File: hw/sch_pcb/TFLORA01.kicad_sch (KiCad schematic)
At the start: 51 parts, among them J1 SM07B-GHS-TB, J2 MCX, U1 MIC5504-3.3YM5, U2 74LVC1G157, U3 SX1262, U4 PE4259, X1 IT3205CE 32MHz

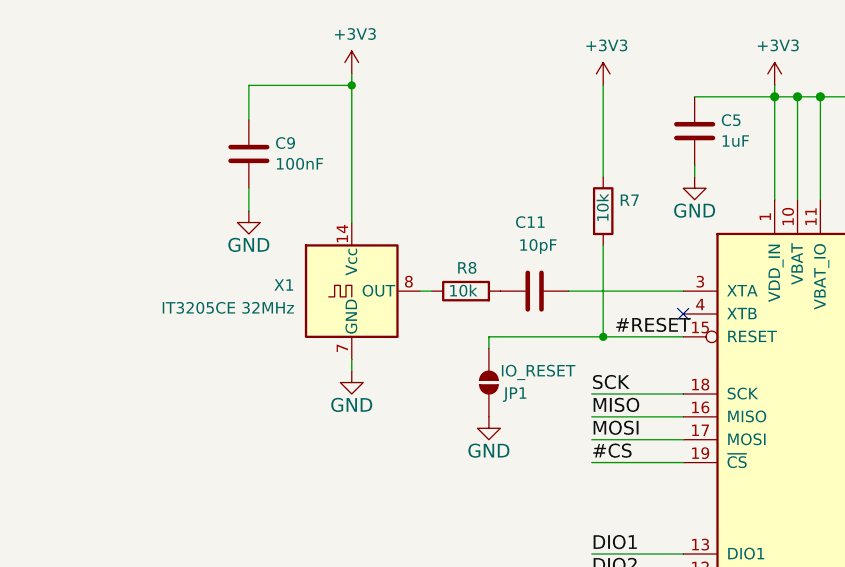
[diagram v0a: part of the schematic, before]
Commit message: Resolve #3 by selecting oscillator.
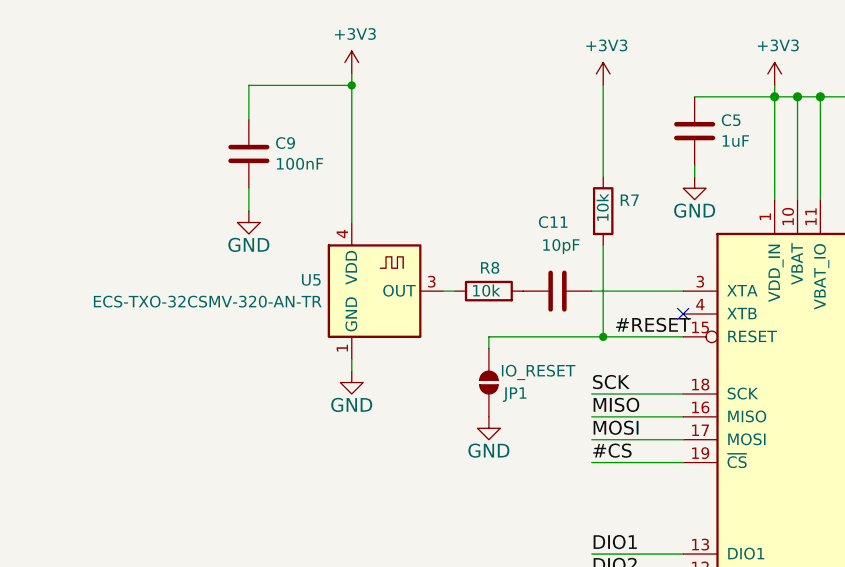
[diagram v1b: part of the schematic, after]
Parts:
- removed X1: IT3205CE 32MHz, Oscillator:Oscillator_DIP-14, symbol Oscillator:TCXO-14
- added U5: ECS-TXO-32CSMV-320-AN-TR, Oscillator:Oscillator_SMD_Abracon_ASE-4Pin_3.2x2.5mm, symbol Oscillator:FT5HN
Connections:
- net +3V3: now also U5.4 (VDD)
- net GND: now also U5.1 (GND), U5.2 (GND)
- net at R8.1: now also U5.3 (OUT)
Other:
- moved on the sheet: C11, R8
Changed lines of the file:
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@@
 	(wire
 		(pts
-			(xy 76.2 91.44) (xy 63.5 91.44)
+			(xy 76.2 91.44) (xy 66.04 91.44)
 		)
 		(stroke
@@
 	(wire
 		(pts
-			(xy 46.99 91.44) (xy 48.26 91.44)
+			(xy 49.53 91.44) (xy 50.8 91.44)
 		)
 		(stroke
@@
 	(symbol
 		(lib_id "ISM02A-rescue:C-Device-ISM02A-rescue")
-		(at 59.69 91.44 90)
+		(at 62.23 91.44 90)
 		(unit 1)
 		(exclude_from_sim no)
@@
 		(dnp no)
 		(property "Reference" "C11"
-			(at 60.96 83.82 90)
+			(at 63.5 83.82 90)
 			(effects
 				(font
@@
 		)
 		(property "Value" "10pF"
-			(at 62.23 86.36 90)
+			(at 64.77 86.36 90)
 			(effects
 				(font
@@
 		)
 		(property "Footprint" "Capacitor_SMD:C_0603_1608Metric"
-			(at 63.5 90.4748 0)
+			(at 66.04 90.4748 0)
 			(effects
 				(font
@@
 		)
 		(property "Datasheet" "~"
-			(at 59.69 91.44 0)
+			(at 62.23 91.44 0)
 			(effects
 				(font
@@
 		)
 		(property "Description" ""
-			(at 59.69 91.44 0)
+			(at 62.23 91.44 0)
 			(effects
 				(font
@@
 	(symbol
 		(lib_id "ISM02A-rescue:R-Device-ISM02A-rescue")
-		(at 52.07 91.44 90)
+		(at 54.61 91.44 90)
 		(unit 1)
 		(exclude_from_sim no)
@@
 		(dnp no)
 		(property "Reference" "R8"
-			(at 53.34 88.9 90)
+			(at 55.88 88.9 90)
 			(effects
 				(font
@@
 		)
 		(property "Value" "10k"
-			(at 53.34 91.44 90)
+			(at 55.88 91.44 90)
 			(effects
 				(font
@@
 		)
 		(property "Footprint" "Resistor_SMD:R_0603_1608Metric"
-			(at 52.07 93.218 90)
+			(at 54.61 93.218 90)
 			(effects
 				(font
@@
 		)
 		(property "Datasheet" "~"
-			(at 52.07 91.44 0)
+			(at 54.61 91.44 0)
 			(effects
 				(font
@@
 		)
 		(property "Description" ""
-			(at 52.07 91.44 0)
+			(at 54.61 91.44 0)
 			(effects
 				(font
@@
 		)
 		(property "UST_ID" "5c70984512875079b91f8962"
-			(at 135.89 182.88 0)
+			(at 138.43 182.88 0)
 			(effects
 				(font
@@
 	)
 	(symbol
+		(lib_id "Oscillator:FT5HN")
+		(at 41.91 91.44 0)
+		(unit 1)
+		(exclude_from_sim no)
+		(in_bom yes)
+		(on_board yes)
+		(dnp no)
+		(fields_autoplaced yes)
+		(property "Reference" "U5"
+			(at 36.0681 90.2278 0)
+			(effects
+				(font
+					(size 1.27 1.27)
+				)
+				(justify right)
+			)
+		)
+		(property "Value" "ECS-TXO-32CSMV-320-AN-TR"
+			(at 36.0681 92.6521 0)
+			(effects
+				(font
+					(size 1.27 1.27)
+				)
+				(justify right)
+			)
+		)
+		(property "Footprint" "Oscillator:Oscillator_SMD_Abracon_ASE-4Pin_3.2x2.5mm"
+			(at 41.91 107.95 0)
+			(effects
+				(font
+					(size 1.27 1.27)
+				)
+				(hide yes)
+			)
+		)
+		(property "Datasheet" "https://eu.mouser.com/datasheet/2/122/ECS_TXO_32CSMV-1663895.pdf"
+			(at 43.18 110.49 0)
+			(effects
+				(font
+					(size 1.27 1.27)
+				)
+				(hide yes)
+			)
+		)
+		(property "Description" "TCXO Oscillators 32.000 MHz MultiVolt TCXO Clipped Sine Wave 1.7 - 3.465V +/-500ppb -40 - +85C 3.2 x 2.5mm 4-SMD"
+			(at 41.91 91.44 0)
+			(effects
+				(font
+					(size 1.27 1.27)
+				)
+				(hide yes)
+			)
+		)
+		(property "UST_ID" ""
+			(at 41.91 91.44 0)
+			(effects
+				(font
+					(size 1.27 1.27)
+				)
+				(hide yes)
+			)
+		)
+		(pin "2"
+		)
+		(pin "4"
+		)
+		(pin "1"
+		)
+		(pin "3"
+		)
+		(instances
+			(project ""
+				(path "/4497622e-6a35-4d56-b145-e61873b6a125"
+					(reference "U5")
+					(unit 1)
+				)
+			)
+		)
+	)
+	(symbol
 		(lib_id "Device:R")
 		(at 44.45 31.75 90)
@@
 					(unit 1)
 				)
-			)
-		)
-	)
-	(symbol
-		(lib_id "Oscillator:TCXO-14")
-		(at 39.37 91.44 0)
-		(unit 1)
-		(exclude_from_sim no)
-		(in_bom yes)
-		(on_board yes)
-		(dnp no)
-		(fields_autoplaced yes)
-		(property "Reference" "X1"
-			(at 33.02 90.805 0)
-			(effects
-				(font
-					(size 1.27 1.27)
-				)
-				(justify right)
-			)
-		)
-		(property "Value" "IT3205CE 32MHz"
-			(at 33.02 93.345 0)
-			(effects
-				(font
-					(size 1.27 1.27)
-				)
-				(justify right)
-			)
-		)
-		(property "Footprint" "Oscillator:Oscillator_DIP-14"
-			(at 50.8 100.33 0)
-			(effects
-				(font
-					(size 1.27 1.27)
-				)
-				(hide yes)
-			)
-		)
-		(property "Datasheet" "http://www.golledge.com/pdf/products/tcxos/gtxos14.pdf"
-			(at 36.83 91.44 0)
-			(effects
-				(font
-					(size 1.27 1.27)
-				)
-				(hide yes)
-			)
-		)
-		(property "Description" ""
-			(at 39.37 91.44 0)
-			(effects
-				(font
-					(size 1.27 1.27)
-				)
-				(hide yes)
-			)
-		)
-		(pin "1"
-		)
-		(pin "14"
-		)
-		(pin "7"
-		)
-		(pin "8"
-		)
-		(instances
-			(project ""
-				(path "/4497622e-6a35-4d56-b145-e61873b6a125"
-					(reference "X1")
-					(unit 1)
-				)

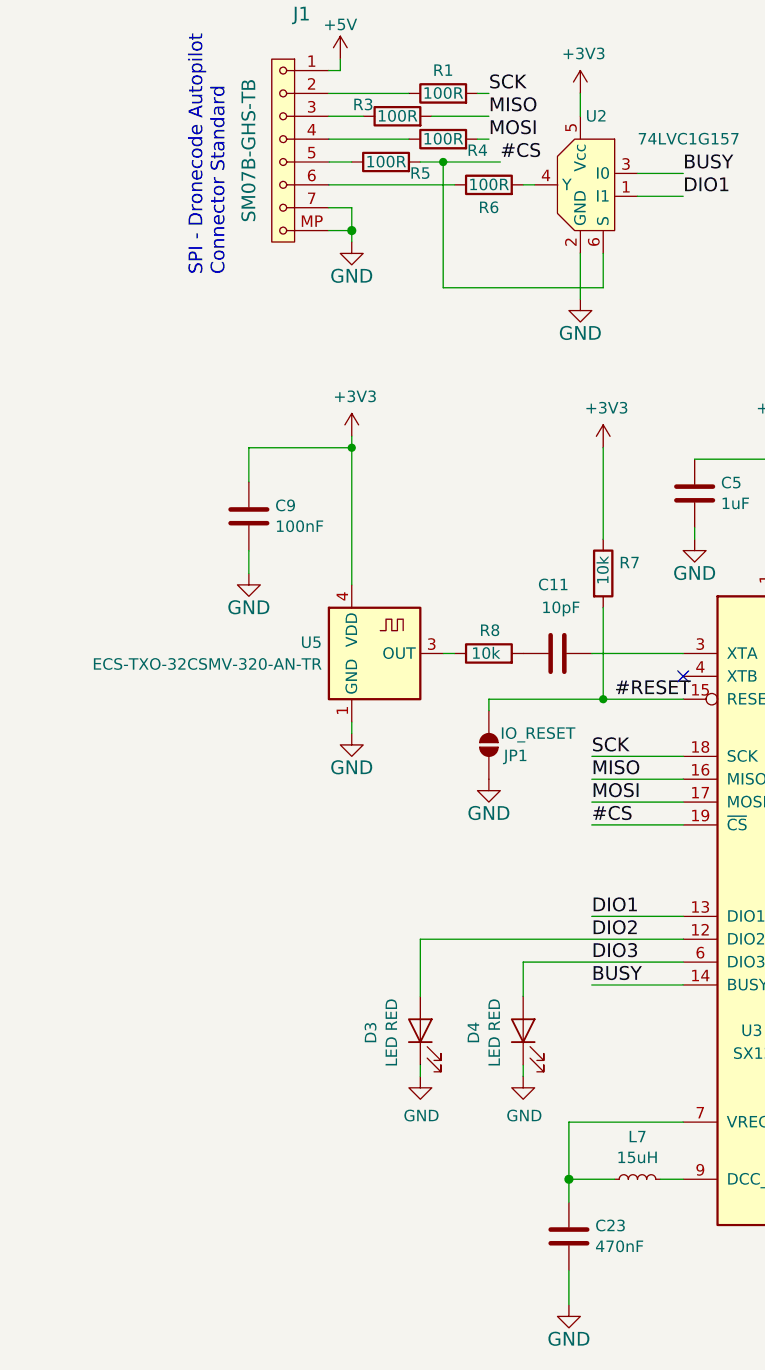
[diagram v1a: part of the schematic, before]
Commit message: Routed PCB, WIP.
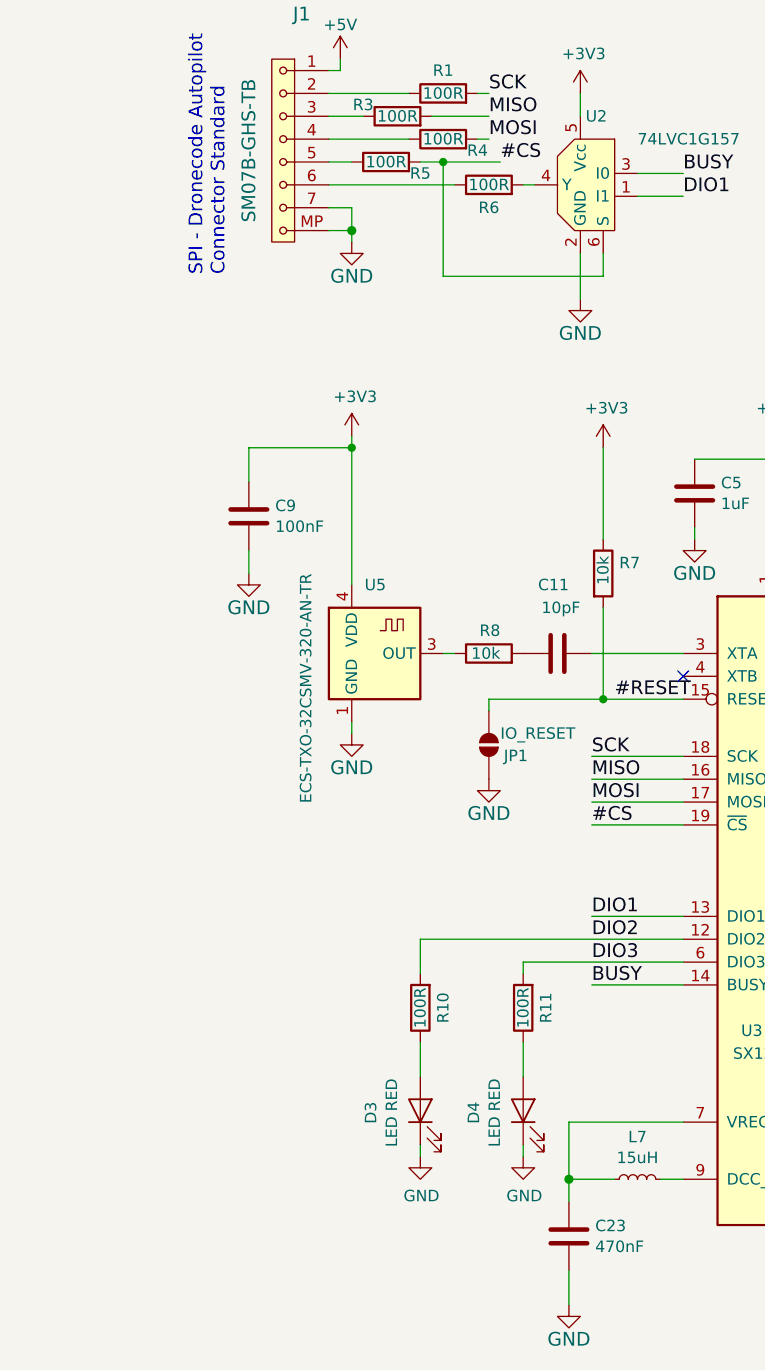
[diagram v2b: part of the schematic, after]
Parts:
- added R10, R11: 100R, Resistor_SMD:R_0603_1608Metric, symbol Device:R
- J2: footprint Mlab_CON:MCX_Molex_73415-1061 -> Mlab_CON:MCX
- JP1: footprint (none) -> Jumper:SolderJumper-2_P1.3mm_Open_RoundedPad1.0x1.5mm
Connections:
- net DIO2: now also R10.2; no longer D3.2 (A)
- net DIO3: now also R11.2; no longer D4.2 (A)
- new net: D4.2 (A), R11.1
- new net: D3.2 (A), R10.1
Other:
- moved on the sheet: D3, D4

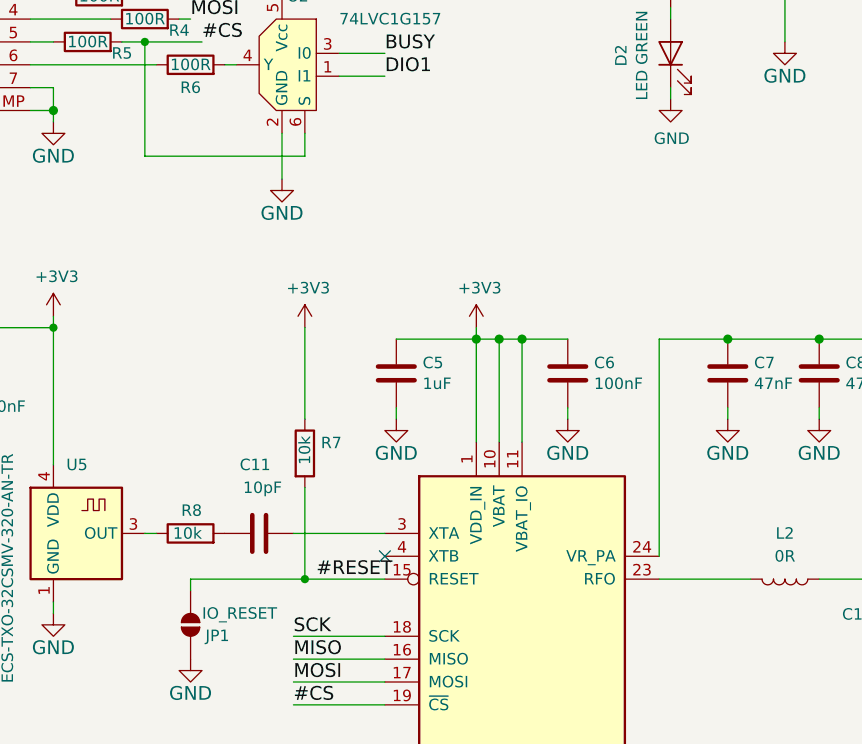
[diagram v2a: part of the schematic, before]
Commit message: Rerouting RF layout. Change 0402 inductors to 0603 for increase of Q.
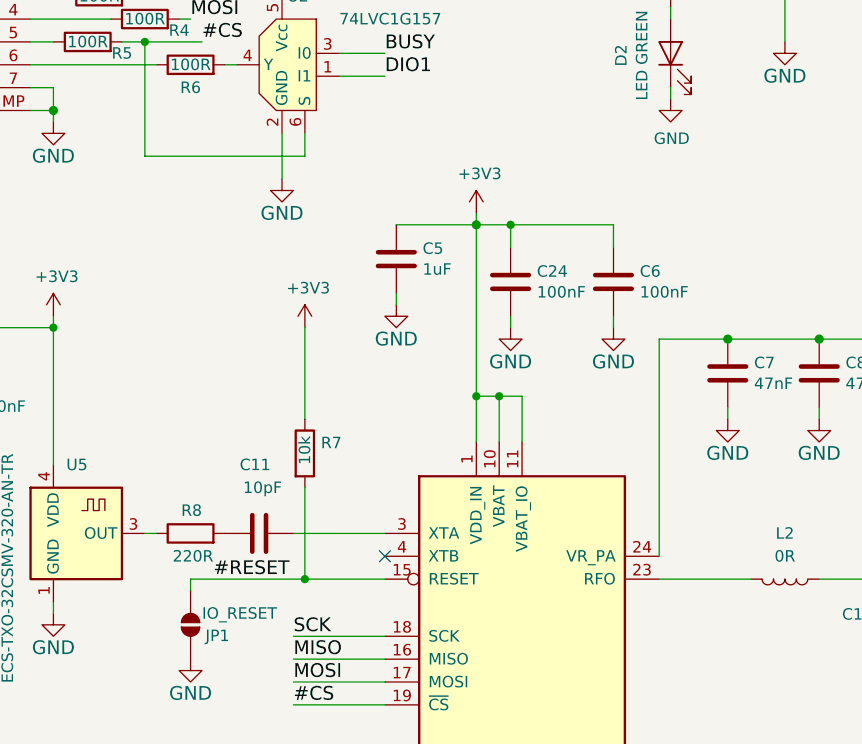
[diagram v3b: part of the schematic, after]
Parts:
- added C24: 100nF, Capacitor_SMD:C_0603_1608Metric, symbol ISM02A-rescue:C-Device-ISM02A-rescue
- L1, L2, L3, L4, L5, L6: footprint Inductor_SMD:L_0402_1005Metric -> Inductor_SMD:L_0603_1608Metric
- R8: value 10k -> 220R
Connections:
- net +3V3: now also C24.1
- net GND: now also C24.2
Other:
- moved on the sheet: C5, C6

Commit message: Adding logo, improving silkscreen. Minor layout improvements. Fix components identification.
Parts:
- added G1: LOGO, MLAB_LOGA:TF, symbol MLAB_TF_LOGO:LOGO
- L1: MFPN LQW15AN47NJ00D -> LQW18AS47NG00D; UST_ID 5dad56ba128750448eca1968 -> 5c70984412875079b91f8813
- L2: UST_ID 5c70984512875079b91f8949 -> 5c70984512875079b91f894e
- L3: value 2n5 -> 2n4; UST_ID 5dad56ff128750448eca1975 -> 67119a34d509c19f2ce8ec7b
- L4: MFPN LQW15AN4N7C00D -> LQW18AN4N7D00D; UST_ID 5dad574f128750448eca1986 -> 671226edd509c19f2ce8ed2d
- L5: MFPN LQW15AN9N1H00D -> LQW18AN9N1D00D; UST_ID 5dad5789128750448eca1995 -> 67122378d509c19f2ce8ecdb
- L6: MFPN LQW15AN15NH00D -> LQW18AN15NJ10D; UST_ID 5dad566c128750448eca1959 -> 671220a9d509c19f2ce8eca2
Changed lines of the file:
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@@
 			)
 		)
-		(property "MFPN" "LQW15AN47NJ00D"
+		(property "MFPN" "LQW18AS47NG00D"
 			(at 133.35 73.66 0)
 			(effects
@@
 			)
 		)
-		(property "UST_ID" "5dad56ba128750448eca1968"
+		(property "UST_ID" "5c70984412875079b91f8813"
 			(at -24.13 148.59 0)
 			(effects
@@
 			)
 		)
-		(property "UST_ID" "5c70984512875079b91f8949"
+		(property "UST_ID" "5c70984512875079b91f894e"
 			(at 218.44 -48.26 0)
 			(effects
@@
 			)
 		)
-		(property "Value" "2n5"
+		(property "Value" "2n4"
 			(at 139.7 99.0346 90)
 			(effects
@@
 			)
 		)
-		(property "UST_ID" "5dad56ff128750448eca1975"
+		(property "UST_ID" "67119a34d509c19f2ce8ec7b"
 			(at 237.49 -67.31 0)
 			(effects
@@
 			)
 		)
-		(property "MFPN" "LQW15AN4N7C00D"
+		(property "MFPN" "LQW18AN4N7D00D"
 			(at 257.81 -87.63 0)
 			(effects
@@
 			)
 		)
-		(property "UST_ID" "5dad574f128750448eca1986"
+		(property "UST_ID" "671226edd509c19f2ce8ed2d"
 			(at 257.81 -87.63 0)
 			(effects
@@
 			)
 		)
-		(property "MFPN" "LQW15AN15NH00D"
+		(property "MFPN" " LQW18AN15NJ10D"
 			(at 252.73 -1.27 0)
 			(effects
@@
 			)
 		)
-		(property "UST_ID" "5dad566c128750448eca1959"
+		(property "UST_ID" "671220a9d509c19f2ce8eca2"
 			(at 252.73 -1.27 0)
 			(effects
@@
 			)
 		)
-		(property "MFPN" "LQW15AN9N1H00D"
+		(property "MFPN" "LQW18AN9N1D00D"
 			(at 327.66 -93.98 0)
 			(effects
@@
 			)
 		)
-		(property "UST_ID" "5dad5789128750448eca1995"
+		(property "UST_ID" "67122378d509c19f2ce8ecdb"
 			(at 327.66 -93.98 0)
 			(effects
@@
 					(unit 1)
 				)
+			)
+		)
+	)
+	(symbol
+		(lib_id "MLAB_TF_LOGO:LOGO")
+		(at 259.08 30.48 0)
+		(unit 1)
+		(exclude_from_sim no)
+		(in_bom no)
+		(on_board yes)
+		(dnp no)
+		(fields_autoplaced yes)
+		(property "Reference" "G1"
+			(at 273.3431 30.959 0)
+			(effects
+				(font
+					(size 1.27 1.27)
+				)
+				(justify left)
+			)
+		)
+		(property "Value" "LOGO"
+			(at 259.08 36.9476 0)
+			(effects
+				(font
+					(size 1.27 1.27)
+				)
+				(hide yes)
+			)
+		)
+		(property "Footprint" "MLAB_LOGA:TF"
+			(at 259.08 30.48 0)
+			(effects
+				(font
+					(size 1.27 1.27)
+				)
+				(hide yes)
+			)
+		)
+		(property "Datasheet" ""
+			(at 259.08 30.48 0)
+			(effects
+				(font
+					(size 1.27 1.27)
+				)
+				(hide yes)
+			)
+		)
+		(property "Description" ""
+			(at 259.08 30.48 0)
+			(effects
+				(font
+					(size 1.27 1.27)
+				)
+				(hide yes)
+			)
+		)
+		(instances
+			(project "TFLORA01"
+				(path "/4497622e-6a35-4d56-b145-e61873b6a125"
+					(reference "G1")
+					(unit 1)
+				)

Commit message: Fix components identification.
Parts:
- C11: UST_ID (none) -> 5c70984812875079b91f8be2
- J2: UST_ID (none) -> 5fa10cc512875025b39779f6
- R8: UST_ID 5c70984512875079b91f8962 -> 5c70984512875079b91f8958
- U2: UST_ID (none) -> 67123367d509c19f2ce8edcb
- U5: UST_ID (none) -> 6712346fd509c19f2ce8ee06
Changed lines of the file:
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@@
 			)
 		)
-		(property "UST_ID" ""
+		(property "UST_ID" "5fa10cc512875025b39779f6"
 			(at 6.35 208.28 0)
 			(effects
@@
 			)
 		)
+		(property "UST_ID" "5c70984812875079b91f8be2"
+			(at 62.23 91.44 0)
+			(effects
+				(font
+					(size 1.27 1.27)
+				)
+				(hide yes)
+			)
+		)
 		(pin "1"
 		)
@@
 			)
 		)
-		(property "UST_ID" "5c70984512875079b91f8962"
+		(property "UST_ID" "5c70984512875079b91f8958"
 			(at 138.43 182.88 0)
 			(effects
@@
 			)
 		)
-		(property "UST_ID" ""
+		(property "UST_ID" "6712346fd509c19f2ce8ee06"
 			(at 41.91 91.44 0)
 			(effects
@@
 			(at 66.04 39.37 0)
 			(effects
+				(font
+					(size 1.27 1.27)
+				)
+				(hide yes)
+			)
+		)
+		(property "UST_ID" "67123367d509c19f2ce8edcb"
+			(at 66.04 39.37 0)
+			(effects

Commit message: Update to KiCADv9.
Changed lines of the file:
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@@
 (kicad_sch
-	(version 20231120)
+	(version 20250114)
 	(generator "eeschema")
-	(generator_version "8.0")
+	(generator_version "9.0")
 	(paper "A4")
 	(title_block
@@
 		(comment 6 "jacho,cernohorsky")
 	)
+	(text "SPI - Dronecode Autopilot\nConnector Standard"
+		(exclude_from_sim no)
+		(at 25.4 49.53 90)
+		(effects
+			(font
+				(size 1.524 1.524)
+			)
+			(justify left bottom)
+		)
+	)
+	(text "POWER INPUT"
+		(exclude_from_sim no)
+		(at 184.785 43.18 0)
+		(effects
+			(font
+				(size 1.524 1.524)
+			)
+			(justify left bottom)
+		)
+	)
 	(junction
 		(at 188.595 24.13)
@@
 		)
 	)
-	(text "SPI - Dronecode Autopilot\nConnector Standard"
-		(exclude_from_sim no)
-		(at 25.4 49.53 90)
-		(effects
-			(font
-				(size 1.524 1.524)
-			)
-			(justify left bottom)
-		)
-	)
-	(text "POWER INPUT"
-		(exclude_from_sim no)
-		(at 184.785 43.18 0)
-		(effects
-			(font
-				(size 1.524 1.524)
-			)
-			(justify left bottom)
-		)
-	)
 	(label "MOSI"
 		(at 66.04 107.95 0)
-		(fields_autoplaced yes)
 		(effects
 			(font
@@
 	(label "DIO1"
 		(at 76.2 40.64 0)
-		(fields_autoplaced yes)
 		(effects
 			(font
@@
 	(label "MISO"
 		(at 66.04 105.41 0)
-		(fields_autoplaced yes)
 		(effects
 			(font
@@
 	(label "BUSY"
 		(at 66.04 128.27 0)
-		(fields_autoplaced yes)
 		(effects
 			(font
@@
 	(label "MOSI"
 		(at 54.61 34.29 0)
-		(fields_autoplaced yes)
 		(effects
 			(font
@@
 	(label "SCK"
 		(at 66.04 102.87 0)
-		(fields_autoplaced yes)
 		(effects
 			(font
@@
 	(label "SCK"
 		(at 54.61 29.21 0)
-		(fields_autoplaced yes)
 		(effects
 			(font
@@
 	(label "#CS"
 		(at 55.88 36.83 0)
-		(fields_autoplaced yes)
 		(effects
 			(font
@@
 	(label "DIO2"
 		(at 226.06 144.78 0)
-		(fields_autoplaced yes)
 		(effects
 			(font
@@
 	(label "#CS"
 		(at 66.04 110.49 0)
-		(fields_autoplaced yes)
 		(effects
 			(font
@@
 	(label "DIO1"
 		(at 66.04 120.65 0)
-		(fields_autoplaced yes)
 		(effects
 			(font
@@
 	(label "MISO"
 		(at 54.61 31.75 0)
-		(fields_autoplaced yes)
 		(effects
 			(font
@@
 	(label "#RESET"
 		(at 57.15 96.52 0)
-		(fields_autoplaced yes)
 		(effects
 			(font
@@
 	(label "BUSY"
 		(at 76.2 38.1 0)
-		(fields_autoplaced yes)
 		(effects
 			(font
@@
 	(label "DIO2"
 		(at 66.04 123.19 0)
-		(fields_autoplaced yes)
 		(effects
 			(font
@@
 	(label "DIO3"
 		(at 66.04 125.73 0)
-		(fields_autoplaced yes)
 		(effects
 			(font
@@
 		)
 	)
+	(embedded_fonts no)
 )

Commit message: Update project workflows.
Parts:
- C19: MFPN C0G 0,1pF 50V -> (none)
- C20: now not fitted
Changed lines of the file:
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@@
-			)
-		)
-		(property "MFPN" "C0G 0,1pF 50V"
-			(at 124.46 130.81 0)
-			(effects
-				(font
-					(size 1.27 1.27)
-				)
-				(hide yes)
 			)
 		)
@@
 		(in_bom yes)
 		(on_board yes)
-		(dnp no)
+		(dnp yes)
 		(property "Reference" "C20"
 			(at 136.271 135.9916 0)
@@
 			(at 133.35 137.16 0)
 			(effects
+				(font
+					(size 1.27 1.27)
+				)
+				(hide yes)
+			)
+		)
+		(property "UST_ID" ""
+			(at 133.35 137.16 0)
+			(effects
